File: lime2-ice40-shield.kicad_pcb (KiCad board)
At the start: 2 copper layers, 53.2 x 59.6 mm, 5 parts

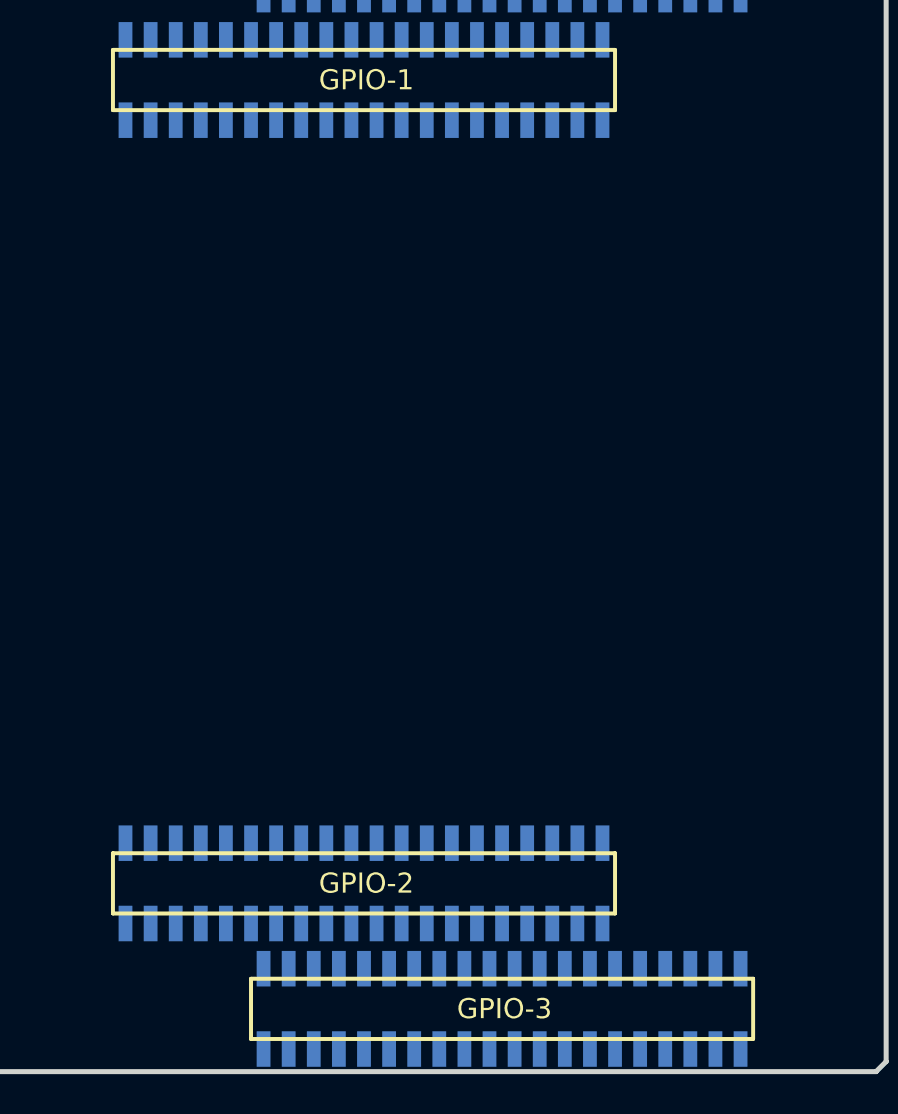
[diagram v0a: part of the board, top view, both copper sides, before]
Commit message: Initial routing of CSI1 signals
Signed-off-by: Rangel Ivanov <rangelivanov88@gmail.com>
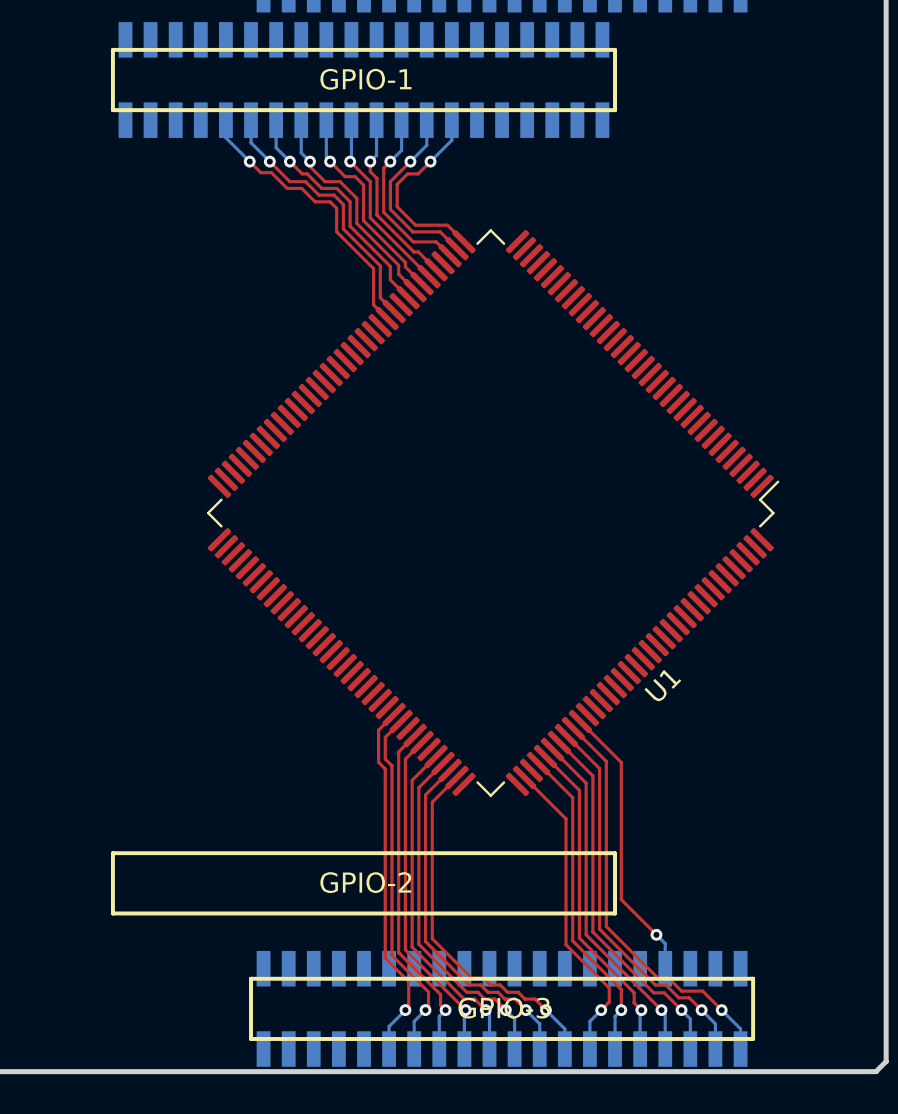
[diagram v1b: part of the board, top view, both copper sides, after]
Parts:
- removed GPIO-2: FL40YA-V36P-2X20-LF, lime2-ice40-shield:YA-V36P-2X20-LF
- added U1: ICE40HX4K-TQ144, lime2-ice40-shield:TQFP-144_20x20mm_P0.5mm, F.Cu at (6.60, 1.52)
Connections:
- net +3.3V renamed +3V3
- net /ECOL/LCD1_HSYNC/ATAIOR/KP_OUT6/SDC1_D2/CSI1_HSYNC/PH26 renamed Net-(GPIO-3-Pad38)
- net /ECRS/LCD1_DE/ATAIORDY/KP_OUT5/SDC1_D1/CSI1_FIELD/PH25 renamed Net-(GPIO-3-Pad36)
- net /EINT12/NCE4/SPI2_CS0/PC19 renamed /SPI2_CS0\C19
- net /EINT13/NCE5/SPI2_CLK/PC20 renamed /SPI2_CLK\PC20
- net /EINT14/NCE6/SPI2_MOSI/PC21 renamed /SPI2_MOSI\PC21
- net /EINT15/NCE7/SPI2_MISO/PC22 renamed /SPI2_MISO\PC22
- net /ERXD3/LCD1_D8/ATAD4/KP_IN0/MS_D0/EINT8/CSI1_D8/PH8 renamed /CSI1_D8\PH8
- net /ETXERR/LCD1_VSYNC/ATAIOW/KP_OUT7/SDC1_D3/CSI1_VSYNC/PH27 renamed Net-(GPIO-3-Pad40)
- net /FMINL renamed Net-(GPIO-4-Pad19)
- net /FMINR renamed Net-(GPIO-4-Pad17)
- net /GNULL/ERXERR/I²S1_MCLK/ERXERR/SPI3_CS1/PA9 renamed Net-(GPIO-4-Pad12)
- net /GNULL/ETXCK/I²S1_BCLK/ETXCK/UART7_TX/UART1_DTR/PA14 renamed Net-(GPIO-4-Pad14)
- net /HPCOM/HPCOMFB renamed Net-(GPIO-1-Pad16)
- net /HPOUTL renamed Net-(GPIO-1-Pad14)
- net /HPOUTR renamed Net-(GPIO-1-Pad18)
- net /I2S_BCLK/AC97_BCLK/PB6 renamed /I2S_BCLK\AC97_BCLK\PB6
- net /I2S_DI/AC97_DI/SPDIF_DI/PB12 renamed /I2S_DI\AC97_DI\SPDIF_DI\PB12
- net /I2S_DO0/AC97_DO/PB8/SATA-PWR-EN renamed /I2S_DO0\AC97_DO\PB8
- net /I2S_DO1/PB9 renamed /I2S_DO1\PB9
- net /I2S_DO2/PB10 renamed /I2S_DO2\PB10
- net /I2S_DO3/PB11 renamed /I2S_DO3\PB11
- net /I2S_LRCK/AC97_SYNC/PB7 renamed /I2S_LRCK\AC97_SYNC\PB7
- net /I2S_MCLK/AC97_MCLK/PB5 renamed /I2S_MCLK\AC97_MCLK\PB5
- net /IR0_RX/PB4 renamed Net-(GPIO-3-Pad6)
- net /IR0_TX/SPDIF_MCLK/STANBYWFI/PB3 renamed Net-(GPIO-3-Pad4)
- net /JTAG_CK0/SPI2_CLK/PB15 renamed Net-(GPIO-3-Pad28)
- net /JTAG_DI0/SPI2_MISO/PB17 renamed Net-(GPIO-3-Pad32)
- net /JTAG_DO0/SPI2_MOSI/PB16 renamed Net-(GPIO-3-Pad30)
- net /JTAG_MS0/SPI2_CS0/PB14 renamed Net-(GPIO-3-Pad26)
- net /LCD0_CLK/SMC_VCCEN/PD24 renamed Net-(LCD_CON1-Pad31)
- net /LCD0_D0/LVDS0_VP0/PD0 renamed Net-(LCD_CON1-Pad21)
- net /LCD0_D1/LVDS0_VN0/PD1 renamed Net-(LCD_CON1-Pad22)
- net /LCD0_D10/LVDS1_VP0/PD10 renamed Net-(LCD_CON1-Pad15)
- net /LCD0_D11/LVDS1_VN0/PD11 renamed Net-(LCD_CON1-Pad16)
- net /LCD0_D12/LVDS1_VP1/PD12 renamed Net-(LCD_CON1-Pad17)
- net /LCD0_D13/LVDS1_VN1/PD13 renamed Net-(LCD_CON1-Pad18)
- net /LCD0_D14/LVDS1_VP2/PD14 renamed Net-(LCD_CON1-Pad19)
- net /LCD0_D15/LVDS1_VN2/PD15 renamed Net-(LCD_CON1-Pad20)
- net /LCD0_D16/LVDS1_VPC/PD16 renamed Net-(LCD_CON1-Pad5)
- net /LCD0_D17/LVDS1_VNC/PD17 renamed Net-(LCD_CON1-Pad6)
- net /LCD0_D18/LVDS1_VP3/PD18 renamed Net-(LCD_CON1-Pad7)
- net /LCD0_D19/LVDS1_VN3/PD19 renamed Net-(LCD_CON1-Pad8)
- net /LCD0_D2/LVDS0_VP1/PD2 renamed Net-(LCD_CON1-Pad23)
- net /LCD0_D20/CSI1_MCLK/PD20 renamed Net-(LCD_CON1-Pad9)
- net /LCD0_D21/SMC_VPPEN/PD21 renamed Net-(LCD_CON1-Pad10)
- net /LCD0_D22/SMC_VPPPP/PD22 renamed Net-(LCD_CON1-Pad11)
- net /LCD0_D23/SMC_DET/PD23 renamed Net-(LCD_CON1-Pad12)
- net /LCD0_D3/LVDS0_VN1/PD3 renamed Net-(LCD_CON1-Pad24)
- net /LCD0_D4/LVDS0_VP2/PD4 renamed Net-(LCD_CON1-Pad25)
- net /LCD0_D5/LVDS0_VN2/PD5 renamed Net-(LCD_CON1-Pad26)
- net /LCD0_D6/LVDS0_VPC/PD6 renamed Net-(LCD_CON1-Pad27)
- net /LCD0_D7/LVDS0_VNC/PD7 renamed Net-(LCD_CON1-Pad28)
- net /LCD0_D8/LVDS0_VP3/PD8 renamed Net-(LCD_CON1-Pad13)
- net /LCD0_D9/LVDS0_VN3/PD9 renamed Net-(LCD_CON1-Pad14)
- net /LCD0_DE/SMC_RST/PD25 renamed Net-(LCD_CON1-Pad32)
- net /LCD0_HSYNC/SMC_SLK/PD26 renamed Net-(LCD_CON1-Pad29)
- net /LCD0_VSYNC/SMC_SDA/PD27 renamed Net-(LCD_CON1-Pad30)
- net /LCD1_D0/ATAA0/UART3_TX/EINT0/CSI1_D0/PH0 renamed Net-(GPIO-3-Pad7)
- net /LCD1_D7/ATAD3/UART5_RX/MS_CLK/EINT7/CSI1_D7/PH7/I2S_DO1/PB9/USB0-DRV renamed Net-(GPIO-3-Pad9)
- net /LINEINL renamed Net-(GPIO-4-Pad15)
- net /LINEINR renamed Net-(GPIO-4-Pad13)
- net /LRADC0 renamed Net-(GPIO-1-Pad6)
- net /LRADC1 renamed Net-(GPIO-1-Pad8)
- net /MIC1OUTN renamed Net-(GPIO-4-Pad8)
- net /MIC1OUTP renamed Net-(GPIO-4-Pad6)
- net /MICIN1 renamed Net-(GPIO-1-Pad10)
- net /MICIN2 renamed Net-(GPIO-4-Pad10)
- net /NC/IR0_RX/PB4 renamed Net-(LCD_CON1-Pad34)
- net /NC/IR0_TX/SPDIF_MCLK/STANBYWFI/PB3 renamed Net-(LCD_CON1-Pad33)
- net /NCE1/PC3/SATA-PWR-EN renamed Net-(GPIO-1-Pad29)
- net /NCE2/PC17 renamed Net-(GPIO-4-Pad20)
- net /NCE3/PC18 renamed Net-(GPIO-1-Pad31)
- net /NDQS/PC24 renamed Net-(GPIO-1-Pad38)
- net /NMI_N renamed Net-(GPIO-4-Pad4)
- net /NRB1/SDC2_CLK/PC7 renamed Net-(GPIO-4-Pad16)
- net /NWP/PC16 renamed Net-(GPIO-4-Pad18)
- net /PB2/PWM0 renamed Net-(LCD_CON1-Pad36)
- net /RESET_N renamed Net-(GPIO-3-Pad5)
- net /SPI0_CS0/PC23 renamed Net-(GPIO-1-Pad40)
- net /SPI2_CS1/SPDIF_DO/PB13 renamed /SPI2_CS1\SPDIF_DO\PB13
- net /TS1_CLK/CSI1_PCLK/SDC1_CMD/PG0 renamed Net-(GPIO-1-Pad5)
- net /TS1_ERR/CSI1_MLCK/SDC1_CLK/PG1 renamed Net-(GPIO-1-Pad7)
- net /TVIN0 renamed Net-(GPIO-4-Pad5)
- net /TVIN1 renamed Net-(GPIO-4-Pad7)
- net /TVIN2 renamed Net-(GPIO-4-Pad9)
- net /TVIN3 renamed Net-(GPIO-4-Pad11)
- net /TVOUT0/VGA-G renamed Net-(GPIO-1-Pad20)
- net /TVOUT1/VGA-B renamed Net-(GPIO-1-Pad22)
- net /TVOUT2/VGA-R renamed Net-(GPIO-1-Pad24)
- net /TVOUT3 renamed Net-(GPIO-4-Pad3)
- net /TWI1_SCK/PB18 renamed Net-(GPIO-1-Pad36)
- net /TWI1_SDA/PB19 renamed Net-(GPIO-1-Pad34)
- net /TWI2_SCK/PB20 renamed Net-(GPIO-1-Pad32)
- net /TWI2_SDA/PB21 renamed Net-(GPIO-1-Pad30)
- net /UART0_RX/IR1_RX/PB23 renamed /UART0_RX\PB23
- net /UART0_TX/IR1_TX/PB22 renamed /UART0_TX\PB22
- net /VMIC renamed Net-(GPIO-1-Pad12)
- net /XN_TP renamed Net-(LCD_CON1-Pad38)
- net /XP_TP renamed Net-(LCD_CON1-Pad37)
- net /YN_TP renamed Net-(LCD_CON1-Pad40)
- net /YP_TP renamed Net-(LCD_CON1-Pad39)
- GPIO-1 pad 11: /TS1_DVLD/CSI1_VSYNC/SDC1_D1/PG3 -> /CSI1_VSYNC\PG3
- GPIO-1 pad 13: /TS1_D0/CSI1_D0/SDC1_D2/CSI0_D8/PG4 -> /CSI1_D0\PG4
- GPIO-1 pad 15: /TS1_D1/CSI1_D1/SDC1_D3/CSI0_D9/PG5 -> /CSI1_D1\PG5
- GPIO-1 pad 17: /TS1_D2/CSI1_D2/UART3_TX/CSI0_D10/PG6 -> /CSI1_D2\PG6
- GPIO-1 pad 19: /TS1_D3/CSI1_D3/UART3_RX/CSI0_D11/PG7 -> /CSI1_D3\PG7
- GPIO-1 pad 21: /TS1_D4/CSI1_D4/UART3_RTS/CSI0_D12/PG8 -> /CSI1_D4\PG8
- GPIO-1 pad 23: /TS1_D5/CSI1_D5/UART3_CTS/CSI0_D13/PG9 -> /CSI1_D5\PG9
- GPIO-1 pad 25: /TS1_D6/CSI1_D6/UART4_TX/CSI0_D14/PG10 -> /CSI1_D6\PG10
- GPIO-1 pad 27: /TS1_D7/CSI1_D7/UART4_RX/CSI0_D15/PG11 -> /CSI1_D7\PG11
- GPIO-1 pad 9: /TS1_SYNC/CSI1_HSYNC/SDC1_D0/PG2 -> /CSI1_HSYNC\PG2
- GPIO-3 pad 11: /ERXD2/LCD1_D9/ATAD5/KP_IN1/MS_D1/EINT9/CSI1_D9/PH9 -> /CSI1_D9\PH9
- GPIO-3 pad 13: /ERXD1/LCD1_D10/ATAD6/KP_IN2/MS_D2/EINT10/CSI1_D10/PH10 -> /CSI1_D10\PH10
- GPIO-3 pad 15: /ERXD0/LCD1_D11/ATAD7/KP_IN3/MS_D3/EINT11/CSI1_D11/PH11 -> /CSI1_D11\PH11
- GPIO-3 pad 17: /LCD1_D12/ATAD8/PS2_SCK1/EINT12/CSI1_D12/PH12 -> /CSI1_D12\PH12
- GPIO-3 pad 19: /LCD1_D13/ATAD9/PS2_SDA1/SMC_RST/EINT13/CSI1_D13/PH13 -> /CSI1_D13\PH13
- GPIO-3 pad 21: /ETXD3/LCD1_D14/ATAD10/KP_IN4/SMC_VPPEN/EINT14/CSI1_D14/PH14 -> /CSI1_D14\PH14
- GPIO-3 pad 23: /ETXD2/LCD1_D15/ATAD11/KP_IN5/SMC_VPPPP/EINT15/CSI1_D15/PH15 -> /CSI1_D15\PH15
- GPIO-3 pad 25: /ETXD1/LCD1_D16/ATAD12/KP_IN6/SMC_DET/EINT16/CSI1_D16/PH16 -> /CSI1_D16\PH16
- GPIO-3 pad 27: /ETXD0/LCD1_D17/ATAD13/KP_IN7/SMC_VCCEN/EINT17/CSI1_D17/PH17 -> /CSI1_D17\PH17
- GPIO-3 pad 29: /ERXCK/LCD1_D18/ATAD14/KP_OUT0/SMC_SLK/EINT18/CSI1_D18/PH18 -> /CSI1_D18\PH18
- GPIO-3 pad 31: /ERXERR/LCD1_D19/ATAD15/KP_OUT1/SMC_SDA/EINT19/CSI1_D19/PH19 -> /CSI1_D19\PH19
- GPIO-3 pad 33: /ERXDV/LCD1_D20/ATAOE/CAN_TX/EINT20/CSI1_D20/PH20 -> /CSI1_D20\PH20
- GPIO-3 pad 34: /ETXCK/LCD1_CLK/ATACS1/KP_OUT4/SDC1_D0/CSI1_PCLK/PH24 -> /CSI1_PCLK\PH24
- GPIO-3 pad 35: /EMDC/LCD1_D21/ATADREQ/CAN_RX/EINT21/CSI1_D21/PH21 -> /CSI1_D21\PH21
- GPIO-3 pad 37: /EMDIO/LCD1_D22/ATADACK/KP_OUT2/SDC1_CMD/CSI1_D22/PH22 -> /CSI1_D22\PH22
- GPIO-3 pad 39: /ETEN/LCD1_D23/ATACS0/KP_OUT3/SDC1_CLK/CSI1_D23/PH23 -> /CSI1_D23\PH23
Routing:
- net /CSI1_D23\PH23: track 0.00 -> 20.7 mm, vias 0 -> 1
- net /CSI1_D22\PH22: track 0.00 -> 19.6 mm, vias 0 -> 1
- net /CSI1_D21\PH21: track 0.00 -> 18.6 mm, vias 0 -> 1
- net /CSI1_D9\PH9: track 0.00 -> 18.3 mm, vias 0 -> 1
- net /CSI1_D16\PH16: track 0.00 -> 18.3 mm, vias 0 -> 1
- net /CSI1_D10\PH10: track 0.00 -> 18.1 mm, vias 0 -> 1
- net /CSI1_D15\PH15: track 0.00 -> 17.9 mm, vias 0 -> 1
- net /CSI1_D14\PH14: track 0.00 -> 17.6 mm, vias 0 -> 1
- net /CSI1_D20\PH20: track 0.00 -> 17.5 mm, vias 0 -> 1
- net /CSI1_D11\PH11: track 0.00 -> 17.3 mm, vias 0 -> 1
- net /CSI1_D13\PH13: track 0.00 -> 17.2 mm, vias 0 -> 1
- net /CSI1_D12\PH12: track 0.00 -> 17.1 mm, vias 0 -> 1
- net /CSI1_D19\PH19: track 0.00 -> 16.8 mm, vias 0 -> 1
- net /CSI1_D18\PH18: track 0.00 -> 16.3 mm, vias 0 -> 1
- net /CSI1_D17\PH17: track 0.00 -> 15.9 mm, vias 0 -> 1
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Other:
- net class Default: clearance 0.254 -> 0.18; trace_width 0.254 -> 0.16; via_dia 0.889 -> 0.6; via_drill 0.635 -> 0.3
- rule pad_to_mask_clearance: 0.2 -> 0.051
- rule trace_clearance: 0.254 -> 0.18
- rule trace_min: 0.254 -> 0.16
- rule via_min_drill: 0.508 -> 0.3
- rule via_min_size: 0.889 -> 0.4

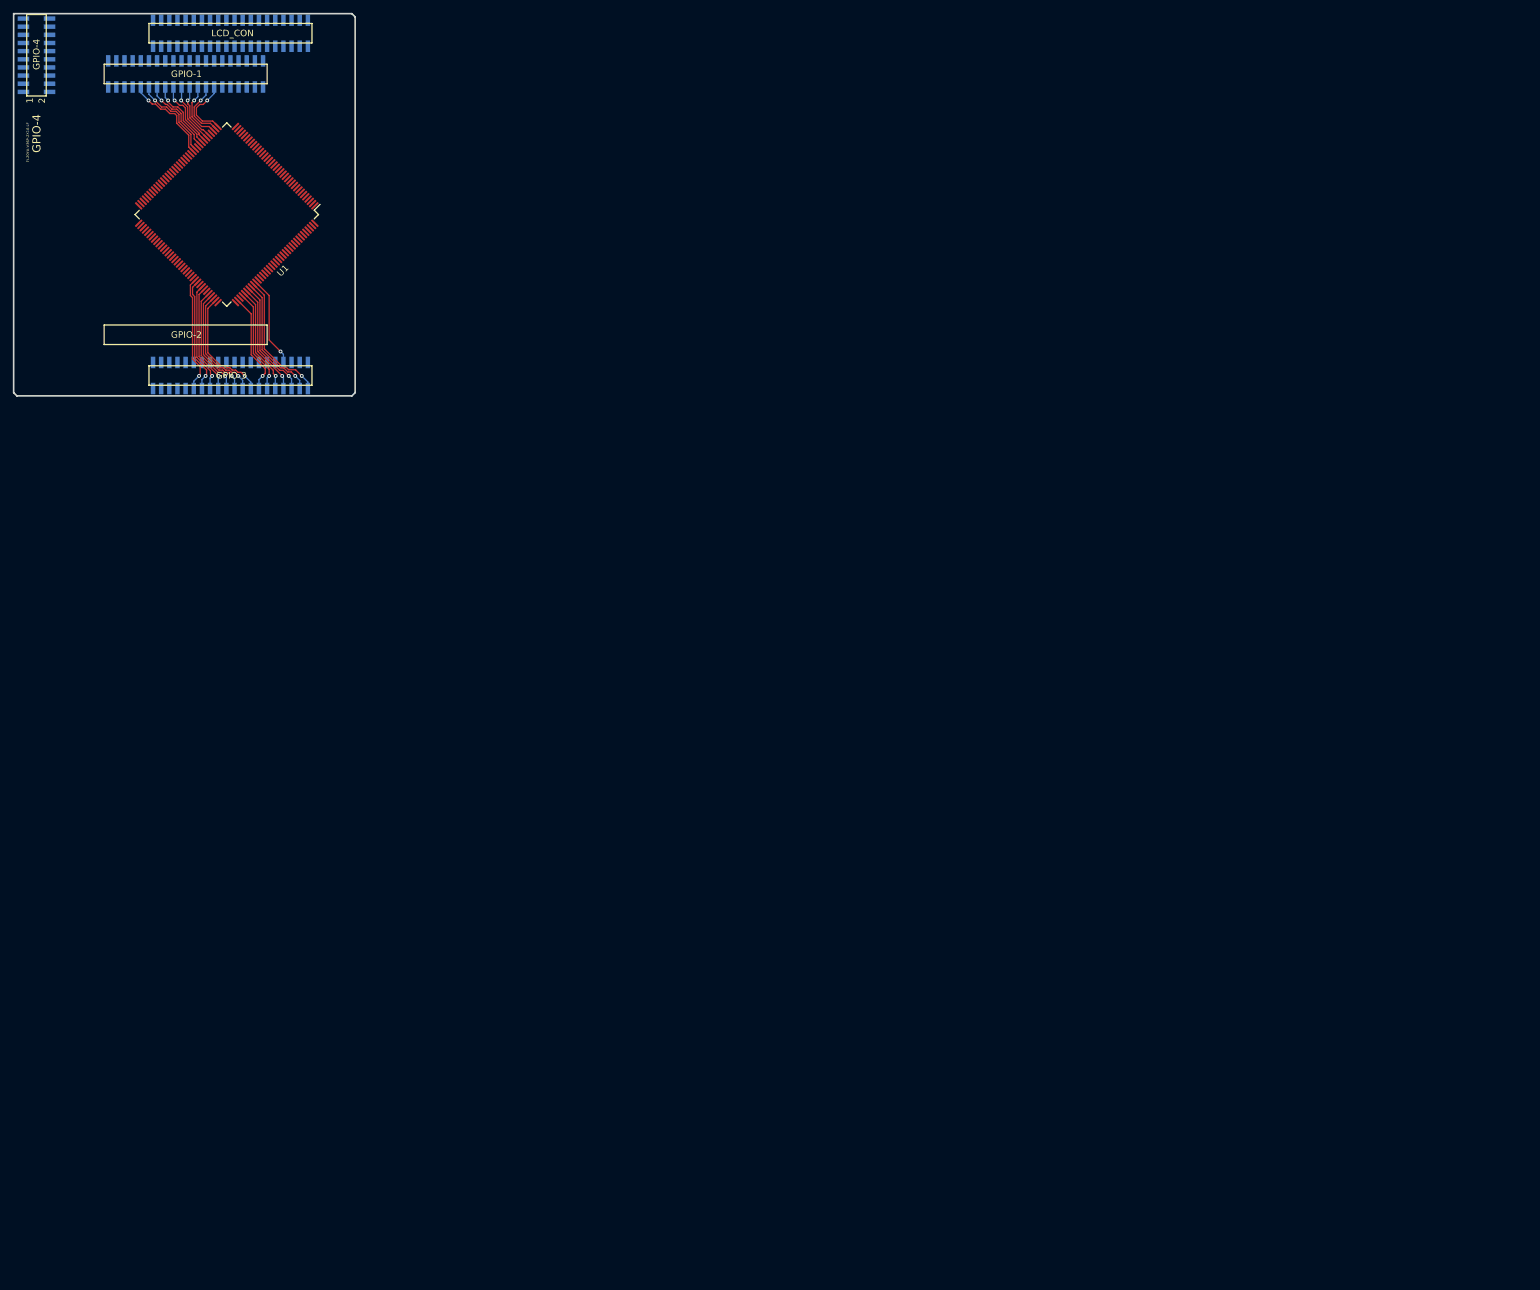
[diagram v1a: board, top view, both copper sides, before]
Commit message: Initial routing of SDRAM
Signed-off-by: Rangel Ivanov <rangelivanov88@gmail.com>
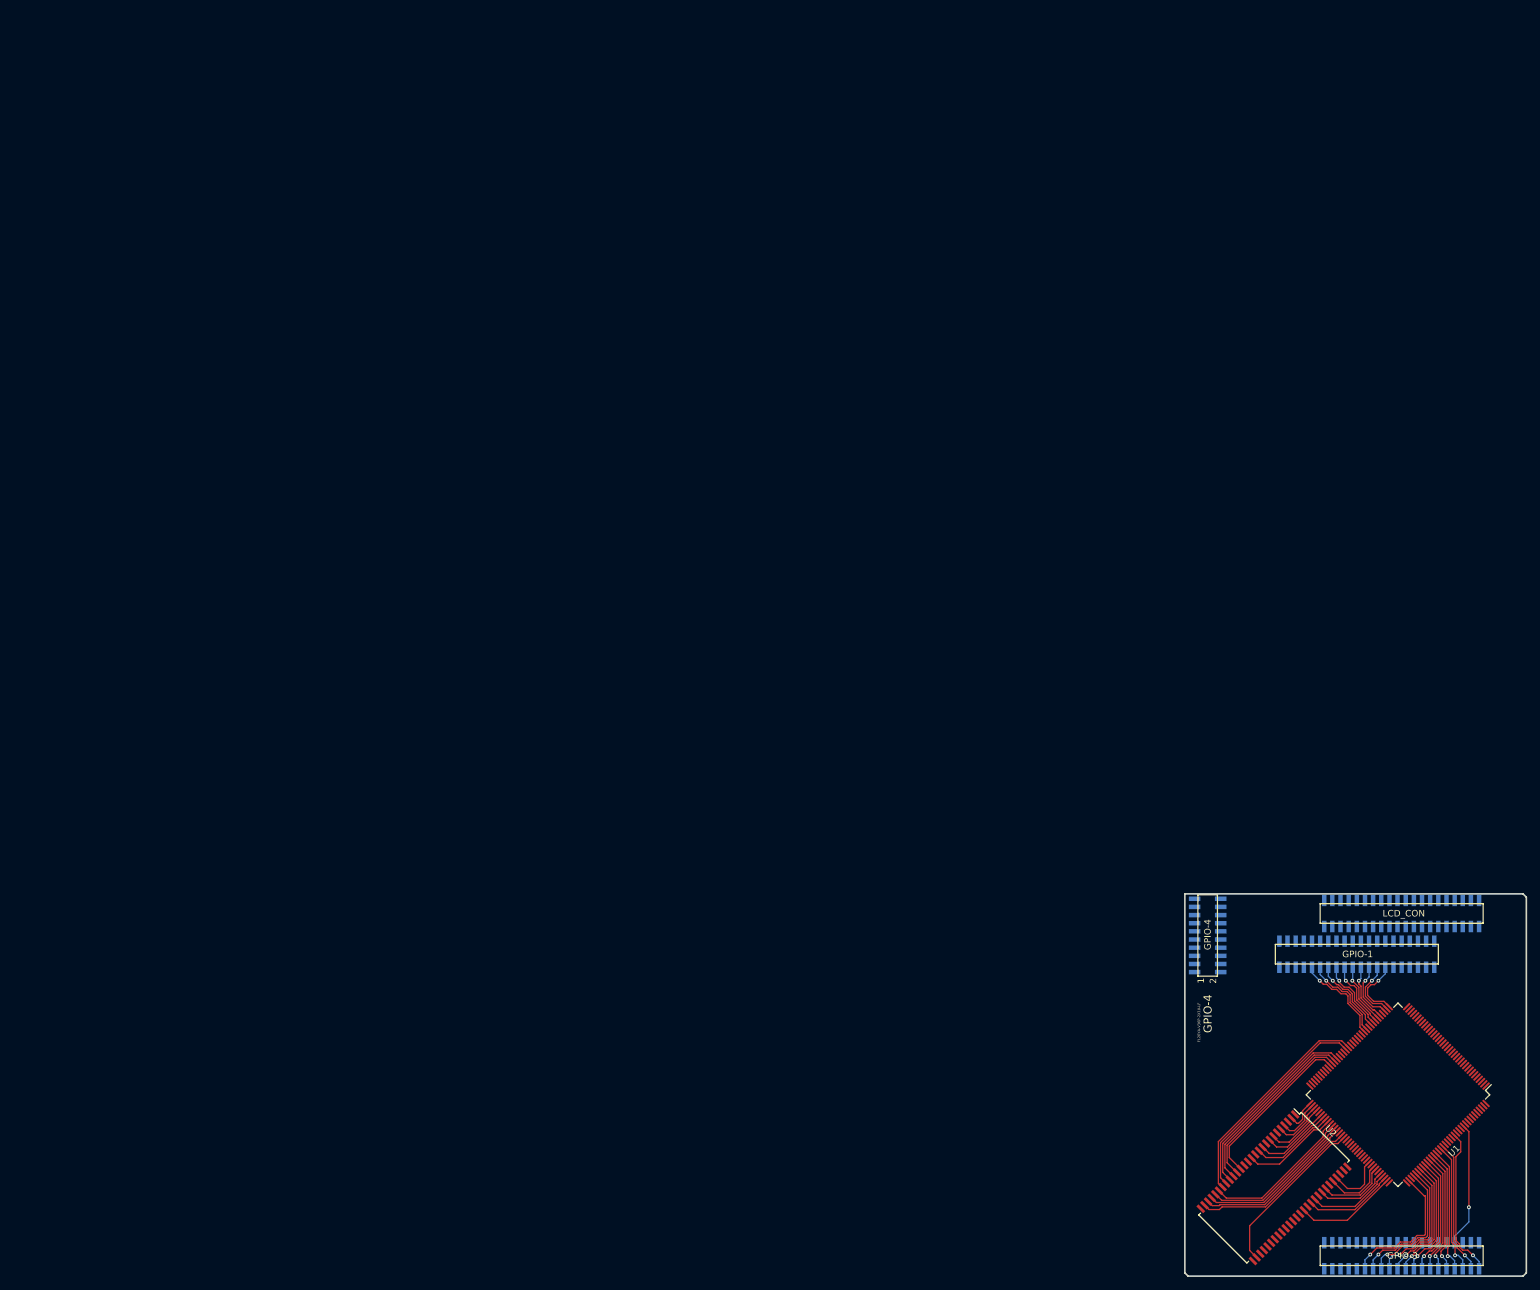
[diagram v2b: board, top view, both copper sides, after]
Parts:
- added U2: AS4C4M16SA-6TCN, lime2-ice40-shield:TSOP-II-54_22.2x10.16mm_P0.8mm, F.Cu at (169.8, 153.2)
- moved GPIO-1 228.3 mm to (182.7, 116.8)
- moved GPIO-3 228.3 mm to (189.7, 163.8)
- moved GPIO-4 228.3 mm to (159.4, 113.9)
- moved LCD_CON1 228.3 mm to (189.7, 110.4)
- moved U1 228.3 mm to (189.1, 138.7)
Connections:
- U1 pad 101: /CSI1_D11\PH11 -> /RAM_DQ13
- U1 pad 102: /CSI1_D12\PH12 -> /RAM_DQ12
- U1 pad 104: /CSI1_D13\PH13 -> /RAM_DQ11
- U1 pad 105: /CSI1_D14\PH14 -> /RAM_DQ10
- U1 pad 106: /CSI1_D15\PH15 -> /RAM_DQ9
- U1 pad 107: /CSI1_D16\PH16 -> /RAM_DQ8
- U1 pad 110: /CSI1_D17\PH17 -> /CSI1_D9\PH9
- U1 pad 112: /CSI1_D18\PH18 -> /CSI1_D10\PH10
- U1 pad 113: /CSI1_D19\PH19 -> /CSI1_D11\PH11
- U1 pad 114: /CSI1_D20\PH20 -> /CSI1_D12\PH12
- U1 pad 115: /CSI1_D21\PH21 -> /CSI1_D13\PH13
- U1 pad 116: /CSI1_D22\PH22 -> /CSI1_D14\PH14
- U1 pad 117: /CSI1_D23\PH23 -> /CSI1_D15\PH15
- U1 pad 118: /CSI1_PCLK\PH24 -> /CSI1_D16\PH16
- U1 pad 119: Net-(U1-Pad119) -> /CSI1_D17\PH17
- U1 pad 120: Net-(U1-Pad120) -> /CSI1_D18\PH18
- U1 pad 121: Net-(U1-Pad121) -> /CSI1_D19\PH19
- U1 pad 122: Net-(U1-Pad122) -> /CSI1_D20\PH20
- U1 pad 124: Net-(U1-Pad124) -> /CSI1_D21\PH21
- U1 pad 125: Net-(U1-Pad125) -> /CSI1_D22\PH22
- U1 pad 130: Net-(U1-Pad130) -> /CSI1_D23\PH23
- U1 pad 134: Net-(U1-Pad134) -> /CSI1_PCLK\PH24
- U1 pad 55: Net-(U1-Pad55) -> /RAM_BA1
- U1 pad 56: Net-(U1-Pad56) -> /RAM_BA0
- U1 pad 60: Net-(U1-Pad60) -> /RAM_CS
- U1 pad 61: Net-(U1-Pad61) -> /RAM_RAS
- U1 pad 62: Net-(U1-Pad62) -> /RAM_CAS
- U1 pad 63: Net-(U1-Pad63) -> /RAM_WE
- U1 pad 73: Net-(U1-Pad73) -> /RAM_DQ0
- U1 pad 74: Net-(U1-Pad74) -> /RAM_DQ1
- U1 pad 75: Net-(U1-Pad75) -> /RAM_DQ2
- U1 pad 76: Net-(U1-Pad76) -> /RAM_DQ3
- U1 pad 78: Net-(U1-Pad78) -> /RAM_DQ4
- U1 pad 79: Net-(U1-Pad79) -> /RAM_DQ5
- U1 pad 80: Net-(U1-Pad80) -> /RAM_DQ6
- U1 pad 81: Net-(U1-Pad81) -> /RAM_DQ7
- U1 pad 82: Net-(U1-Pad82) -> /RAM_A10
- U1 pad 83: Net-(U1-Pad83) -> /RAM_A0
- U1 pad 84: Net-(U1-Pad84) -> /RAM_A1
- U1 pad 85: Net-(U1-Pad85) -> /RAM_A2
- U1 pad 87: Net-(U1-Pad87) -> /RAM_A3
- U1 pad 88: Net-(U1-Pad88) -> /RAM_A4
- U1 pad 90: Net-(U1-Pad90) -> /RAM_CKE
- U1 pad 91: Net-(U1-Pad91) -> /RAM_CLK
- U1 pad 93: Net-(U1-Pad93) -> /RAM_A11
- U1 pad 94: Net-(U1-Pad94) -> /RAM_A9
- U1 pad 95: Net-(U1-Pad95) -> /RAM_A8
- U1 pad 96: Net-(U1-Pad96) -> /RAM_A7
- U1 pad 97: Net-(U1-Pad97) -> /RAM_A6
- U1 pad 98: /CSI1_D9\PH9 -> /RAM_A5
- U1 pad 99: /CSI1_D10\PH10 -> /RAM_DQ14
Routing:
- net /RAM_BA1: track 0.00 -> 34.6 mm
- net /RAM_BA0: track 0.00 -> 33.2 mm
- net /RAM_CS: track 0.00 -> 30.2 mm
- net /RAM_RAS: track 0.00 -> 28.8 mm
- net /RAM_CAS: track 0.00 -> 27.4 mm
- net /RAM_A3: track 0.00 -> 26.5 mm
- net /RAM_WE: track 0.00 -> 26.0 mm
- net /RAM_A4: track 0.00 -> 25.8 mm
- net /RAM_A2: track 0.00 -> 25.3 mm
- net /RAM_A1: track 0.00 -> 24.5 mm
- net /RAM_A0: track 0.00 -> 23.8 mm
- net /RAM_A10: track 0.00 -> 23.2 mm
- net /RAM_DQ8: track 0.00 -> 16.2 mm
- net /RAM_DQ7: track 0.00 -> 15.0 mm
- net /RAM_DQ9: track 0.00 -> 14.1 mm
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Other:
- board text removed: "GPIO-2"
